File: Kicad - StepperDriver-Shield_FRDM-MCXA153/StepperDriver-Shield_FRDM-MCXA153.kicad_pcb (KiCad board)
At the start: 4 copper layers, 91.4 x 54.6 mm, 68 parts, among them J1 Conn_01x02_Socket, J10 Conn_01x03, J11 Conn_01x03, J12 Conn_01x02_Pin, J13 Conn_01x04_Pin, J14 Conn_01x03, J15 Conn_01x03, J16 Conn_01x02_Pin, J17 Conn_01x04_Pin, J18 Conn_01x03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

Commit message: Update 3D Models
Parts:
- removed R21: 0, Resistor_SMD:R_0805_2012Metric_Pad1.20x1.40mm_HandSolder
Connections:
- J5 pad 12: unconnected-(J5-Pin_12-Pad12) -> /P2-12/SCK1
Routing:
- net Net-(J16-Pin_1): track 86.5 -> 74.2 mm, vias 4 -> 3
- net /P2-13/SDO1: track 73.1 -> 71.7 mm
- net GND: vias 15 -> 16

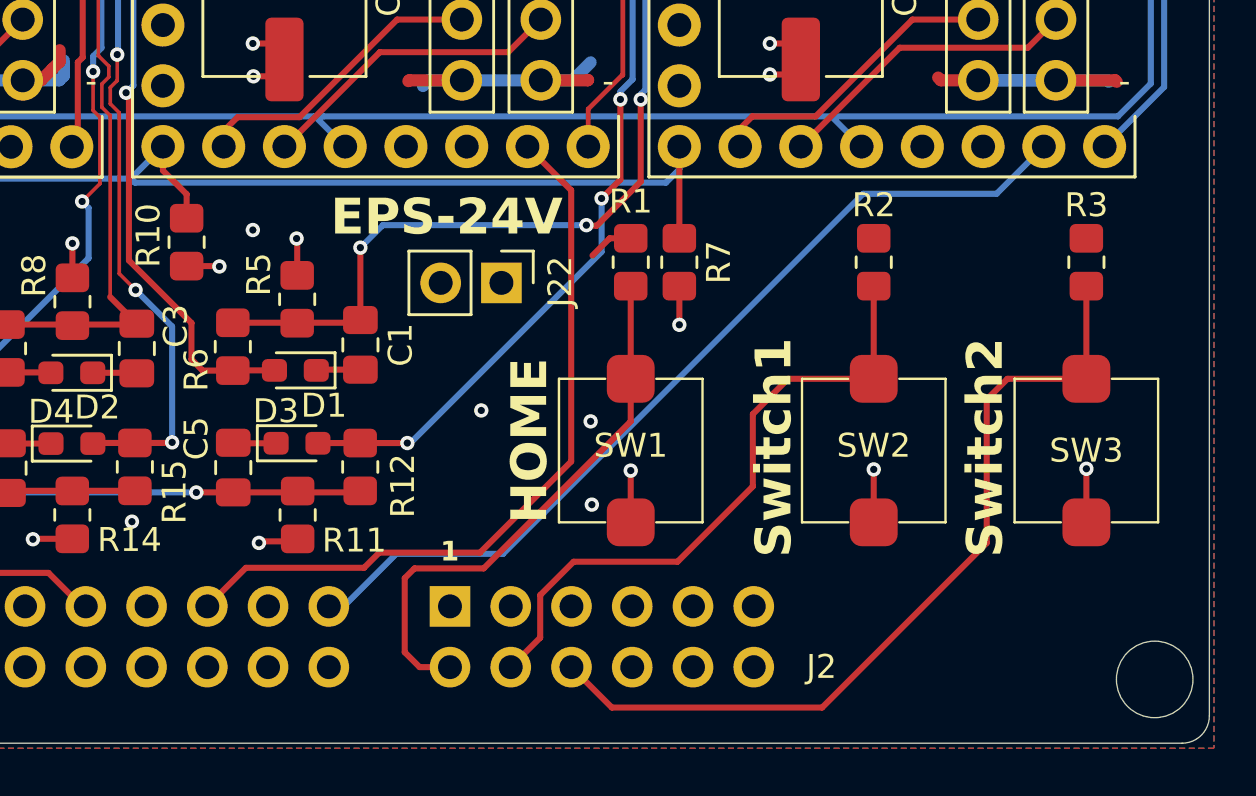
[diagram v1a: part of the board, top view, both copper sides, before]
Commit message: Added Status RGB LED
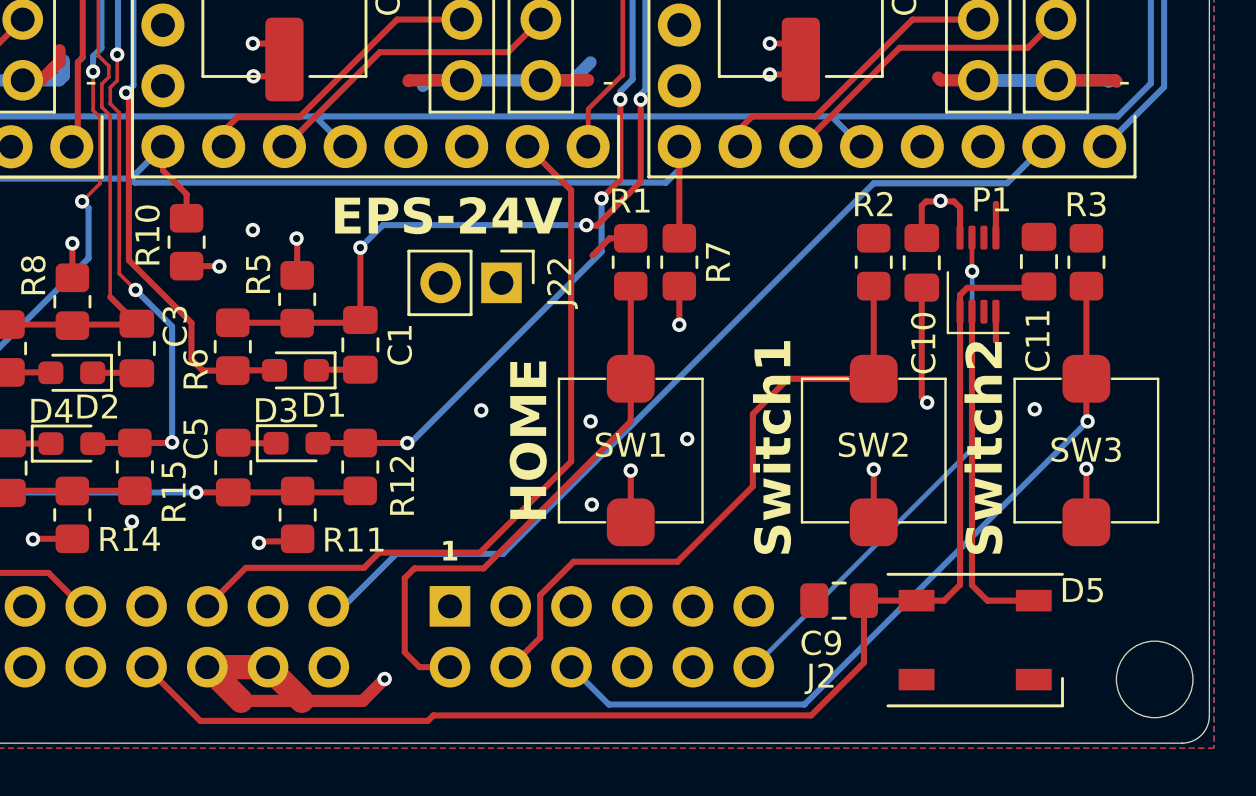
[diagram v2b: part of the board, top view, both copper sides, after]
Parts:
- added C10: 0.1µF, Capacitor_SMD:C_0805_2012Metric_Pad1.18x1.45mm_HandSolder, F.Cu at (164.6, 102.6)
- added C11: 0.1µF, Capacitor_SMD:C_0805_2012Metric_Pad1.18x1.45mm_HandSolder, F.Cu at (169.5, 102.6)
- added C9: 0.1µF, Capacitor_SMD:C_0805_2012Metric_Pad1.18x1.45mm_HandSolder, F.Cu at (161.1, 116.8)
- added D5: WS2812B, LED_SMD:LED_WS2812B_PLCC4_5.0x5.0mm_P3.2mm, F.Cu at (166.8, 118.4)
- added P1: SN74LXC2T45QDCURQ1_, Pegelwandler:SN74LXC2T45QDCURQ1, F.Cu at (166.2, 104.7)
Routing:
- net SYS-5V: track 0.00 -> 54.4 mm
- net /P3-30/ADC0-A13: track 0.00 -> 21.7 mm, vias 0 -> 1
- net GND: track 100.0 -> 120.5 mm, vias 16 -> 20
- net Net-(D5-DIN): track 0.00 -> 14.3 mm
- net Vcc_Logic: track 152.2 -> 156.6 mm, vias 11 -> 12
- net /P1-13/ADC0-A11: track 35.3 -> 32.8 mm, vias 0 -> 1
